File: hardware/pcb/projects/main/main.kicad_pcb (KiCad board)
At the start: 4 copper layers, 100 x 100 mm, 180 parts, among them J1 IO_CON_ANALOG, J10 FX6_DIGITAL, J11 VOICE3_DIGITAL, J12 FX3_DIGITAL, J13 VOICE7_DIGITAL, J14 FX7_DIGITAL, J15 IO_CON_MIDI, J16 VOICE4_DIGITAL, J17 FX4_DIGITAL, J18 VOICE8_DIGITAL, J19 FX8_DIGITAL, J2 PDR_ON_SEL, J20 SWD_CON, J21 MIXER_DIGITAL, J22 DISPLAY1_DIGITAL, J23 IO_CON_DIGITAL, J24 POWER_CON, J25 CONTROL_DIGTAL, J26 DISPLAY2_DIGITAL, J3 VOICE1_DIGITAL, J4 FX1_DIGITAL, J5 VOICE5_DIGITAL, J6 FX5_DIGITAL, J7 VOICE2_DIGITAL, J8 FX2_DIGITAL, J9 VOICE6_DIGITAL, Q1 MMBT3904, Q2 MMBT3904, U1 TL072, U10 AS4C16M16SA, U11 MB85RS2MT, U12 L7803, U2 PCM3060, U3 TL072, U4 74AHCT1G125, U7 74AHCT1G125, U8 STM32F446ZETx, U9 TL072, Y1 8MHz

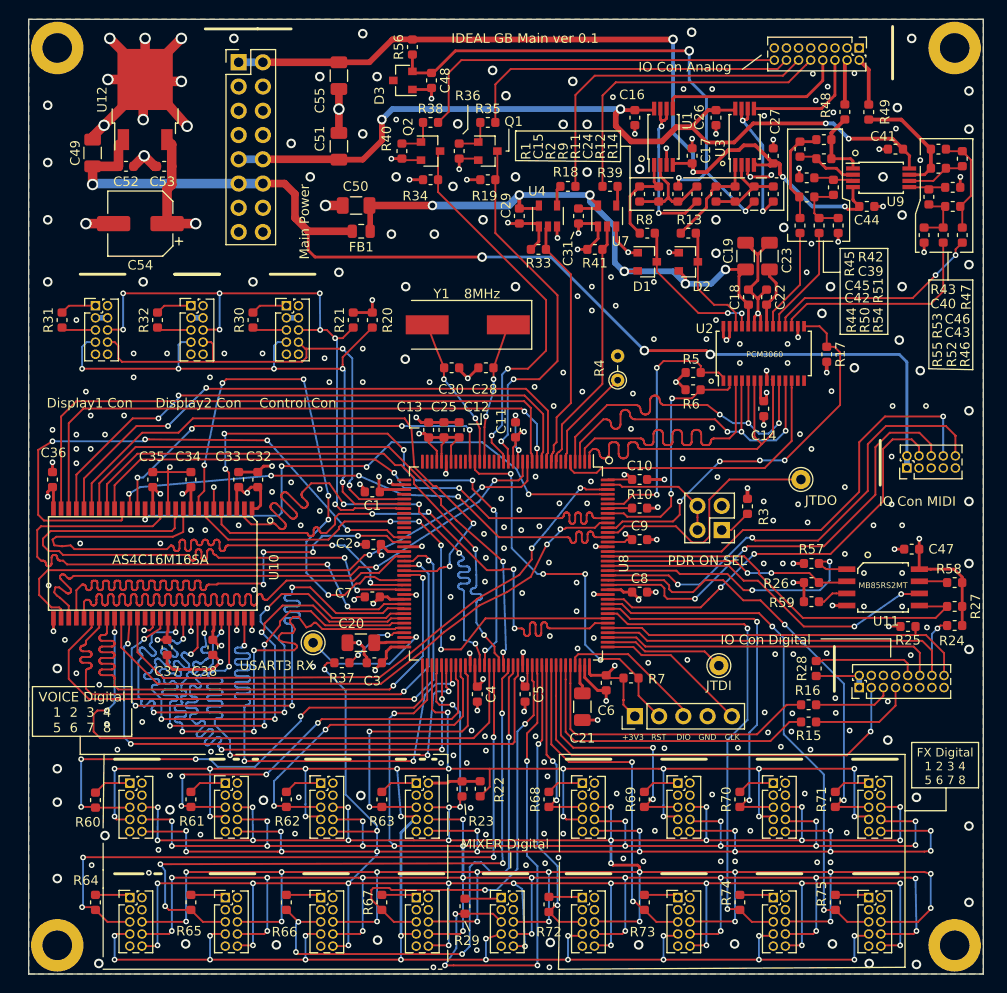
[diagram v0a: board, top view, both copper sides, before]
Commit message: add connector margin on pcb layout
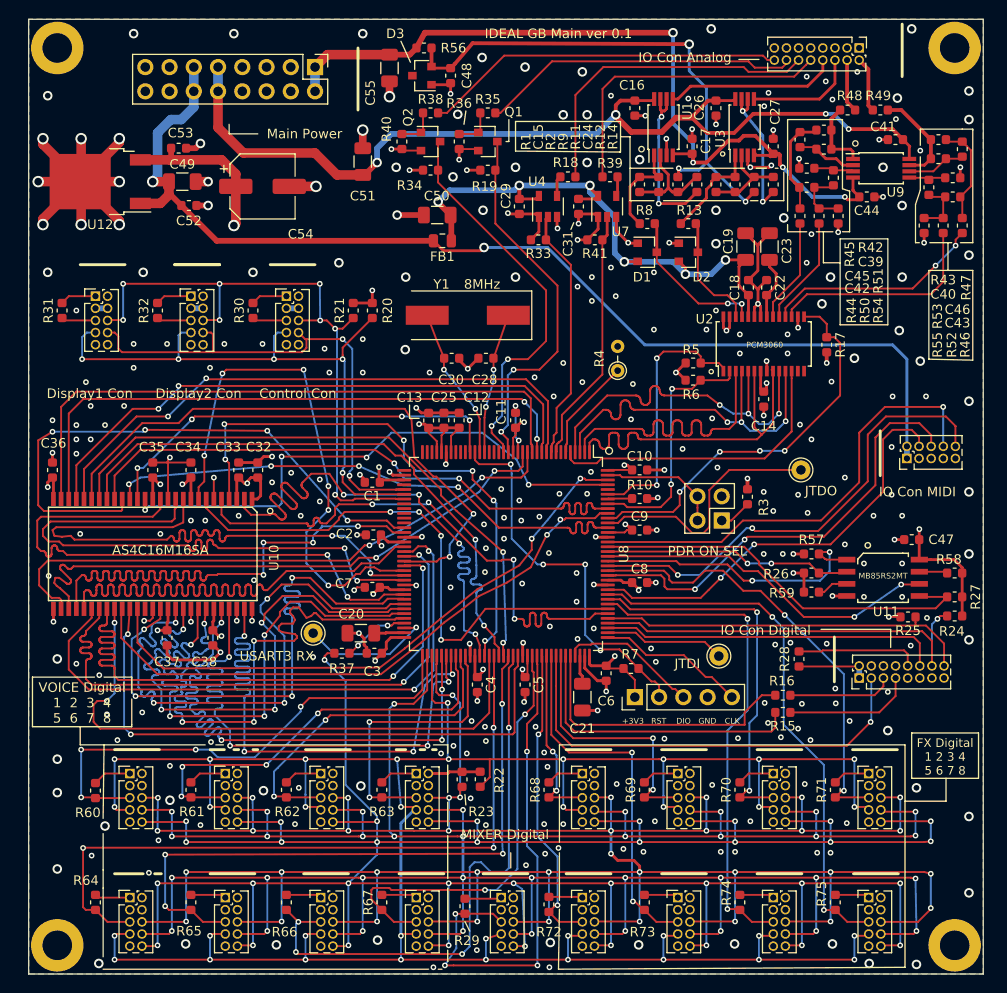
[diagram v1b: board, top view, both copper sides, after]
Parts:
- moved C54 13.4 mm to (74.5, 67.5), turned to 0 degrees
- moved C49 9.87 mm to (66.1, 67.0), turned to 0 degrees
- moved U12 9.80 mm to (57.5, 67.0), turned to 180 degrees
- moved C50 8.56 mm to (92.8, 70.5)
- moved FB1 8.56 mm to (93.3, 73.2)
- moved J24 8.02 mm to (80.0, 55.0), turned to 270 degrees
- moved C52 7.76 mm to (66.8, 69.5)
- moved C55 5.36 mm to (87.8, 55.1)
- moved C51 2.97 mm to (85.0, 64.9)
- moved R15 2.88 mm to (129.0, 122.6)
- moved R16 2.88 mm to (129.0, 120.8)
- moved C53 2.43 mm to (65.7, 63.5), turned to 0 degrees
- moved C48 2.06 mm to (94.2, 55.9)
- moved D3 2.06 mm to (91.2, 55.9)
- moved R28 2.06 mm to (130.7, 117.0)
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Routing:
- net +12V: track 90.8 -> 100.7 mm
- net +3V3: track 791.9 -> 797.4 mm
- net +5VA: track 67.0 -> 62.0 mm
- net -12V: track 91.1 -> 86.1 mm
- net +5V: track 119.0 -> 116.0 mm, vias 4 -> 2
- net /OTG_FS_DP: track 8.30 -> 11.0 mm
- net /OTG_FS_DM: track 10.9 -> 13.6 mm
- net GATE1_IN: track 40.3 -> 37.9 mm
- net Net-(C40-Pad2): track 12.3 -> 10.3 mm
- net GATE2_IN: track 35.5 -> 33.5 mm
- net Net-(R16-Pad2): track 32.4 -> 30.4 mm
- net /~SD_SPI_CS: track 11.0 -> 12.8 mm
- net Net-(R15-Pad2): track 32.9 -> 31.1 mm
- net VREF_-10V: track 56.7 -> 55.0 mm
- net CV1_IN: track 19.7 -> 18.1 mm
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
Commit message: fix pcb layout
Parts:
- moved R23 0.20 mm to (95.6, 129.6)
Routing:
- net /FMC_SDNWE: track 43.8 -> 58.6 mm
- net /FMC_D7: track 60.8 -> 62.8 mm
- net /FMC_A2: track 63.7 -> 62.2 mm
- net /FMC_SDNCAS: track 58.1 -> 59.1 mm
- net /FMC_SDNRAS: track 60.2 -> 59.5 mm
- net /FMC_A8: track 63.2 -> 62.6 mm
- net /FMC_D6: track 61.4 -> 62.0 mm
- net GND: track 204.0 -> 204.5 mm, vias 318 -> 317
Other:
- board text added: "ON OFF"
- board text added: "PDR_SEL"
- board text removed: "PDR ON SEL"
